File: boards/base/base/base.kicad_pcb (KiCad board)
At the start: 2 copper layers, 75 x 71 mm, 17 parts, among them J1 Conn_01x04_Female, J2 Conn_01x06_Female, J3 Conn_01x06_Female, Q1 BC547, Q2 BC547, Q3 2SD1047, U2 ESP32-S3-DevKitC

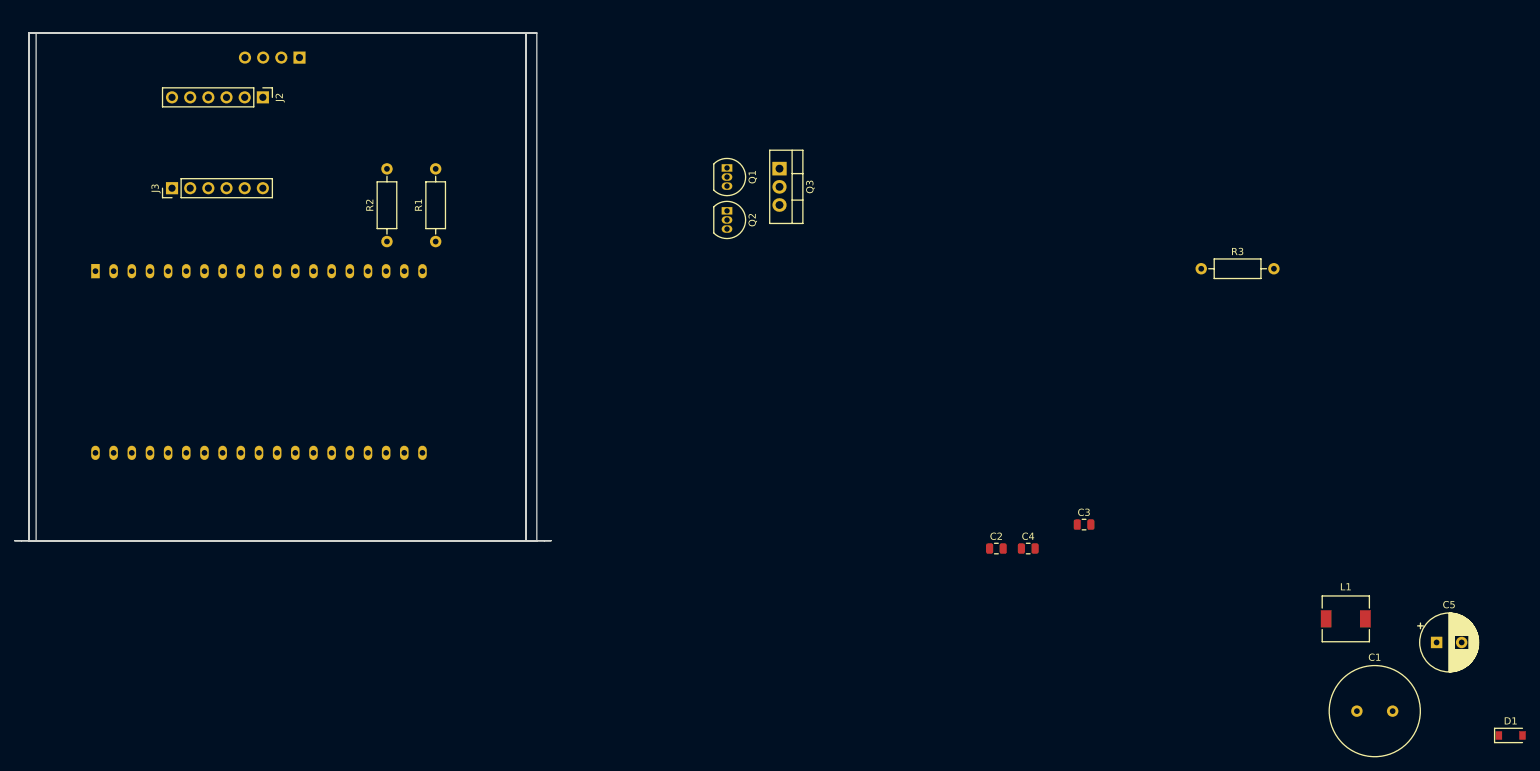
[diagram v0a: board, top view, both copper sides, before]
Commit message: Finished BasePCB
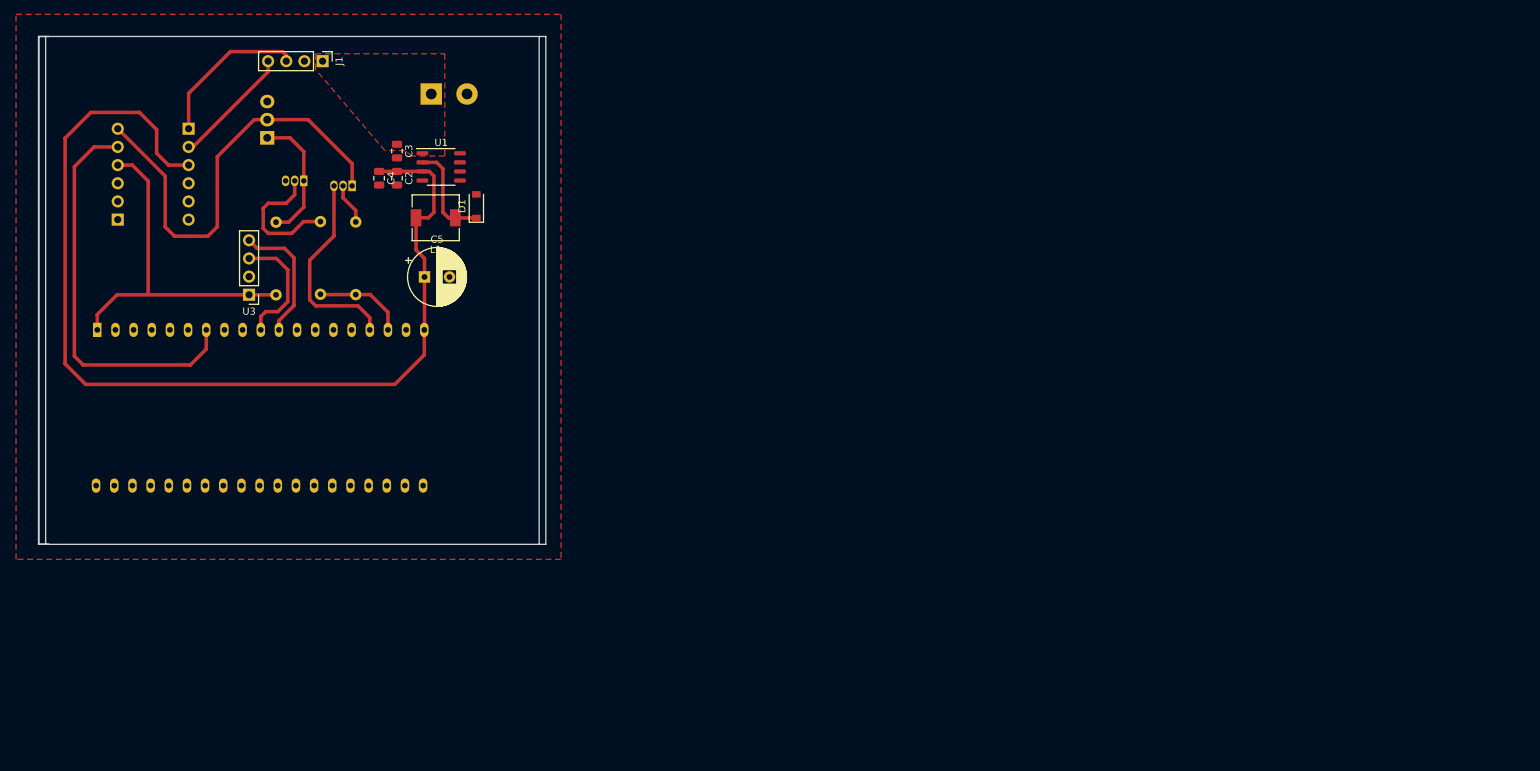
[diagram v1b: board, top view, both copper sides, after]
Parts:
- removed C1: 470uF, Capacitor_THT:C_Radial_D12.5mm_H20.0mm_P5.00mm
- added J4: Screw_Terminal_01x02, TerminalBlock_Altech:Altech_AK300_1x02_P5.00mm_45-Degree, B.Cu at (124.1, 54.3)
- added U1: XL1509-5.0, StackCabinet:XLE1509, F.Cu at (125.5, 64.5)
- added U3: MPU-6050, Connector_PinHeader_2.54mm:PinHeader_1x04_P2.54mm_Vertical, F.Cu at (98.6, 82.4)
- J1: moved to F.Cu
- J2, J3, Q1, Q2, Q3, R1, R2, R3: moved to B.Cu
- moved D1 162.4 mm to (130.4, 70.0), turned to 90 degrees
- moved C5 150.4 mm to (123.1, 79.9)
- moved L1 139.0 mm to (124.7, 71.6), turned to 180 degrees
- moved R3 129.4 mm to (102.4, 82.4), turned to 90 degrees
- moved C3 109.3 mm to (119.3, 62.3), turned to -90 degrees
- moved C4 104.5 mm to (116.8, 66.1), turned to -90 degrees
- moved C2 98.5 mm to (119.3, 66.1), turned to -90 degrees
- moved Q3 71.7 mm to (101.2, 60.5), turned to 90 degrees
- moved Q1 59.2 mm to (106.3, 66.5), turned to 180 degrees
- moved Q2 52.5 mm to (113.0, 67.2), turned to 180 degrees
- moved R1 17.7 mm to (108.6, 82.3)
- moved J2 11.3 mm to (90.2, 59.2), turned to 180 degrees
- moved J3 8.77 mm to (80.3, 71.9), turned to 0 degrees
- moved R2 8.60 mm to (113.5, 82.4)
- moved U2 8.21 mm to (77.4, 87.3)
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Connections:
- J2 pad 3: VBUS -> 5V
- J3 pad 4: LV -> 3V3
- U2 pad 10: unconnected-(U2-Pad10) -> SCL
- U2 pad 11: unconnected-(U2-Pad11) -> SDA
- U2 pad 19: VBUS -> 5V
- U2 pad 32: unconnected-(U2-Pad32) -> GND
- U2 pad 35: GND -> unconnected-(U2-Pad35)
- U2 pad 38: unconnected-(U2-Pad38) -> GND
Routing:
- net 5V: track 0.00 -> 143.9 mm
- net GDA_L: track 0.00 -> 61.3 mm
- net LV2: track 0.00 -> 56.2 mm
- net 3V3: track 0.00 -> 49.2 mm
- net Rx: track 0.00 -> 28.5 mm
- net GDA_H: track 0.00 -> 22.0 mm
- net Net-(Q1-Pad2): track 0.00 -> 18.9 mm
- net Net-(Q1-Pad1): track 0.00 -> 18.4 mm
- net SDA: track 0.00 -> 18.3 mm
- net SCL: track 0.00 -> 17.8 mm
- net SEL0: track 0.00 -> 17.0 mm
- net Net-(D1-Pad1): track 0.00 -> 14.3 mm
- net Tx: track 0.00 -> 12.9 mm
- net Net-(Q2-Pad2): track 0.00 -> 5.78 mm
- added copper zone on F.Cu, net GND
- added copper zone on F.Cu, net VBUS
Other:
- board size 75 x 71 mm -> 70.9 x 71 mm
